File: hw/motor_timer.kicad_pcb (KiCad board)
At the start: 2 copper layers, 15 parts, among them J1 BAT+, J2 BAT-, J3 StartBtn, J4 Motor+, J5 Motor-, Q1 IRF7413, U1 PIC12F1571-I/P

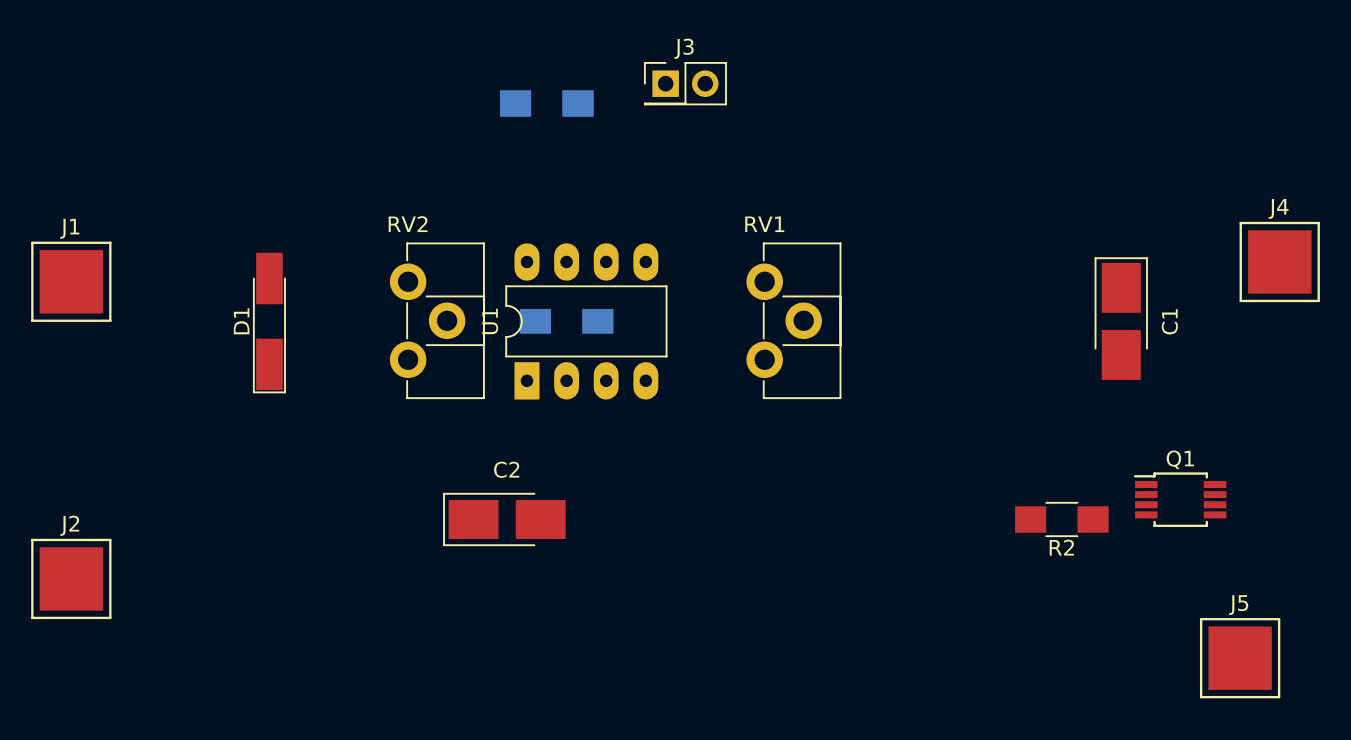
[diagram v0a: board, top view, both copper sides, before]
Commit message: Routed PCB with routes on wrong layers
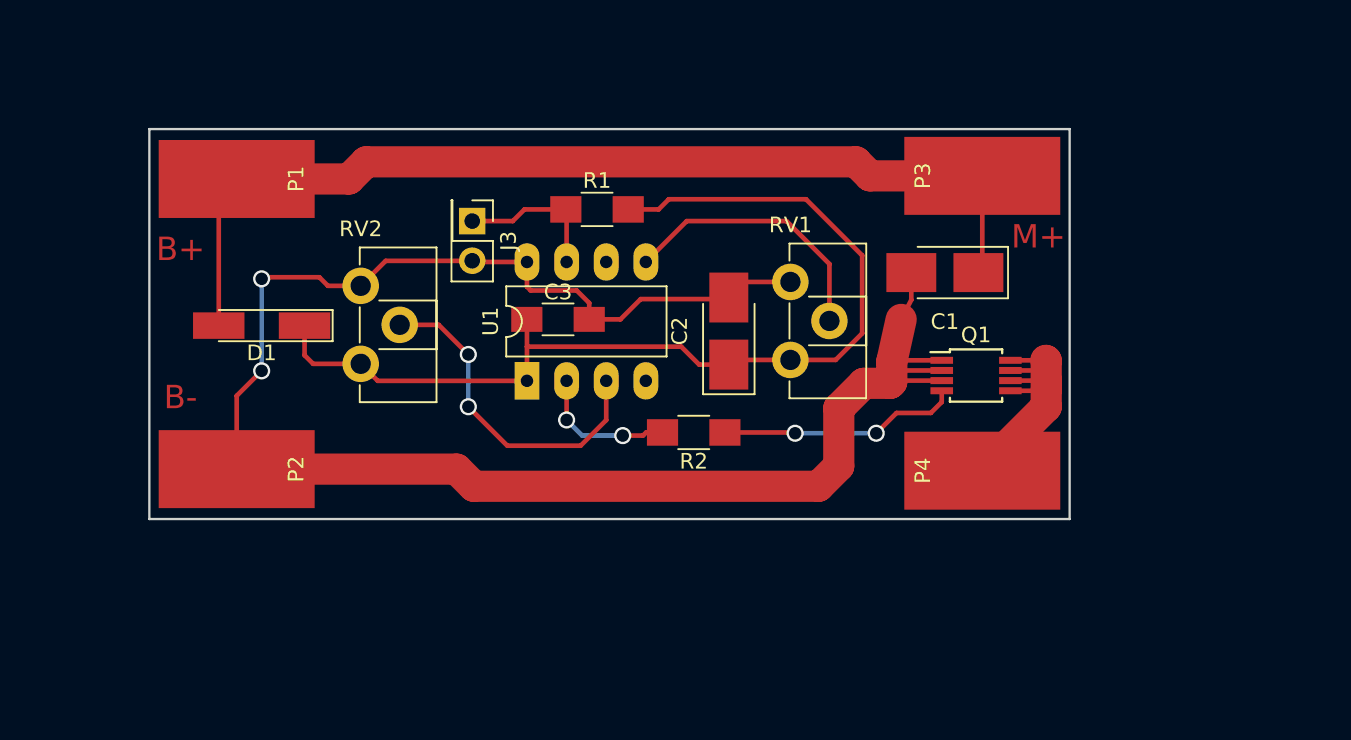
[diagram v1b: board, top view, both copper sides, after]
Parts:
- removed J1: BAT+, SMD_Packages:1Pin
- removed J2: BAT-, SMD_Packages:1Pin
- removed J4: Motor+, SMD_Packages:1Pin
- removed J5: Motor-, SMD_Packages:1Pin
- added P1: BAT+, Wire_Pads:SolderWirePad_single_SMD_5x10mm, F.Cu at (137.6, 91.2)
- added P2: BAT-, Wire_Pads:SolderWirePad_single_SMD_5x10mm, F.Cu at (137.6, 109.8)
- added P3: MOTOR+, Wire_Pads:SolderWirePad_single_SMD_5x10mm, F.Cu at (185.4, 91.0)
- added P4: MOTOR-, Wire_Pads:SolderWirePad_single_SMD_5x10mm, F.Cu at (185.4, 109.9)
- C3, R1: moved to F.Cu
- moved R2 24.3 mm to (166.9, 107.5)
- moved C2 18.7 mm to (169.2, 101.0), turned to 90 degrees
- moved Q1 15.3 mm to (185.0, 103.8)
- moved J3 15.2 mm to (152.7, 93.9), turned to 270 degrees
- moved C1 11.7 mm to (183.0, 97.2), turned to 180 degrees
- moved R1 7.51 mm to (160.7, 93.2), turned to 0 degrees
- moved RV2 3.05 mm to (145.6, 98.0)
- moved RV1 1.65 mm to (173.1, 97.8)
- moved D1 0.57 mm to (139.2, 100.6), turned to 180 degrees
- moved C3 0.57 mm to (158.2, 100.2)
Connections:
- R1 pad 2: Net-(C1-Pad1) -> Net-(C2-Pad1)
- RV1 pad 3: Net-(C1-Pad1) -> Net-(C2-Pad1)
- RV2 pad 3: Net-(C1-Pad1) -> Net-(C2-Pad1)
- U1 pad 4: Net-(U1-Pad4) -> (no net)
- U1 pad 6: Net-(U1-Pad6) -> (no net)
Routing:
- net GND: track 0.00 -> 117.2 mm, vias 0 -> 2
- net Net-(C2-Pad1): track 0.00 -> 65.4 mm
- net Net-(C1-Pad1): track 0.00 -> 64.8 mm
- net Net-(RV2-Pad2): track 0.00 -> 21.6 mm, vias 0 -> 2
- net Net-(P4-Pad1): track 0.00 -> 18.3 mm
- net Net-(RV1-Pad2): track 0.00 -> 17.6 mm
- net Net-(Q1-Pad4): track 0.00 -> 15.5 mm, vias 0 -> 2
- net Net-(J3-Pad1): track 0.00 -> 9.70 mm
- net Net-(R2-Pad2): track 0.00 -> 9.16 mm, vias 0 -> 2
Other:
- board outline added: 59 x 25 mm
- net class Default: clearance 0.2 -> 0; trace_width 0.25 -> 0.3; via_dia 0.6 -> 1.1; via_drill 0.4 -> 0.8
- net class Power added: clearance 0, trace_width 1, via_dia 1.1, via_drill 0.8
- rule trace_clearance: 0.2 -> 0
- board text added: "B+"
- board text added: "B-"
- board text added: "M+"

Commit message: A bit broken small PCB
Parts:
- added J3: StartBtn, Pin_Headers:Pin_Header_Straight_2x01_Pitch2.54mm, F.Cu at (157.3, 120.2)
- added P1: BAT+, Wire_Pads:SolderWirePad_single_SMD_5x10mm, F.Cu at (157.3, 120.2)
- added P2: BAT-, Wire_Pads:SolderWirePad_single_SMD_5x10mm, F.Cu at (157.3, 120.2)
- added P3: MOTOR+, Wire_Pads:SolderWirePad_single_SMD_5x10mm, F.Cu at (157.3, 120.2)
- added P4: MOTOR-, Wire_Pads:SolderWirePad_single_SMD_5x10mm, F.Cu at (157.3, 120.2)
- added P5: Prog, Connectors:GS3, B.Cu at (145.0, 99.4)
- added Throt: Throt, Potentiometers:Potentiometer_Trimmer_Vishay_TS53YJ, F.Cu at (167.1, 99.4)
- added Time: Time, Potentiometers:Potentiometer_Trimmer_Vishay_TS53YJ, F.Cu at (151.0, 99.6)
- C3, D1, Q1, R1, R2: moved to B.Cu
- RV1, RV2: footprint Potentiometers:Potentiometer_Trimmer_ACP_CA9h2.5_Vertical_Px2.5mm_Py5.0mm -> Potentiometers:Potentiometer_Trimmer_Vishay_TS53YJ
- U1: footprint Housings_DIP:DIP-8_W7.62mm_LongPads -> Housings_SOIC:SOIC-8_3.9x4.9mm_Pitch1.27mm; moved to B.Cu
- moved C1 36.8 mm to (146.3, 99.5), turned to 270 degrees
- moved RV1 27.4 mm to (157.3, 120.2)
- moved RV2 25.1 mm to (157.3, 120.2)
- moved D1 22.2 mm to (159.5, 91.5)
- moved Mot- 20.3 mm to (165.3, 107.0)
- moved Mot+ 20.1 mm to (165.3, 92.1)
- moved Q1 19.7 mm to (165.3, 105.0)
- moved Bat- 12.0 mm to (149.3, 107.0)
- moved Bat+ 11.7 mm to (149.3, 92.1)
- moved Start 11.3 mm to (156.9, 104.4)
- moved C2 10.1 mm to (159.2, 98.9), turned to 180 degrees
- moved R1 9.00 mm to (152.1, 95.8), turned to 180 degrees
- moved R2 8.06 mm to (167.2, 99.4), turned to 90 degrees
- moved C3 5.63 mm to (159.4, 94.7), turned to 180 degrees
- moved U1 5.49 mm to (159.3, 99.6), turned to 180 degrees
- renumbered P1 to Bat+, P2 to Bat-, P3 to Mot+, P4 to Mot-, J3 to Start
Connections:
- net Net-(C1-Pad1) renamed +BATT
- net Net-(C2-Pad1) renamed +3V3
- U1 pad 4: (no net) -> Net-(P5-Pad1)
- U1 pad 6: (no net) -> Net-(P5-Pad2)
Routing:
- net GND: track 117.2 -> 60.2 mm, vias 2 -> 1
- net +BATT: track 64.8 -> 26.5 mm, vias 0 -> 1
- net +3V3: track 65.4 -> 41.8 mm, vias 0 -> 1
- net Net-(P5-Pad1): track 0.00 -> 18.7 mm, vias 0 -> 2
- net Net-(RV2-Pad2): track 21.6 -> 5.58 mm, vias 2 -> 1
- net Net-(J3-Pad1): track 9.70 -> 22.2 mm
- net Net-(RV1-Pad2): track 17.6 -> 5.65 mm, vias 0 -> 1
- net Net-(P5-Pad2): track 0.00 -> 11.9 mm
- net Net-(Q1-Pad4): track 15.5 -> 5.52 mm, vias 2 -> 0
- net Net-(R2-Pad2): track 9.16 -> 5.85 mm, vias 2 -> 0
- net Net-(P4-Pad1): track 18.3 -> 15.9 mm, vias 0 -> 1
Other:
- board size 59 x 25 mm -> 27 x 21 mm
- net class Default: clearance 0 -> 0.1778; trace_width 0.3 -> 0.25; via_dia 1.1 -> 0.7; via_drill 0.8 -> 0.4
- net class Power: clearance 0 -> 0.2
- rule trace_clearance: 0 -> 0.1778
- rule trace_min: 0.2 -> 0.1524
- rule via_min_drill: 0.3 -> 0.254
- rule via_min_size: 0.4 -> 0.508
- board text added: "Dat Clk Rst"
- board text added: "Mot tmr v1.0"
- board text added: "v1.0"
- board text removed: "B+"
- board text removed: "B-"
- board text removed: "M+"

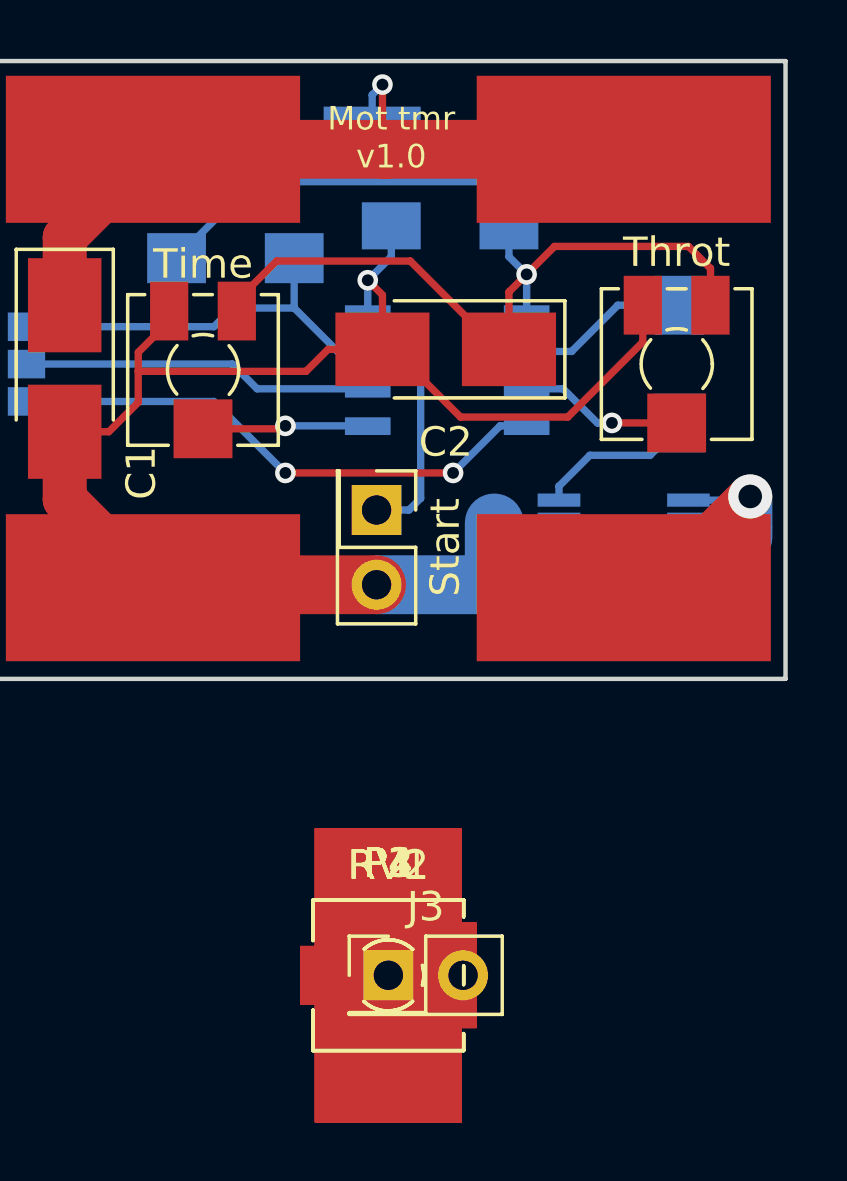
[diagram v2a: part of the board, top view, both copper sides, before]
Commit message: Final version of small PCB. But there are broken referneces betveen schamatic and board.
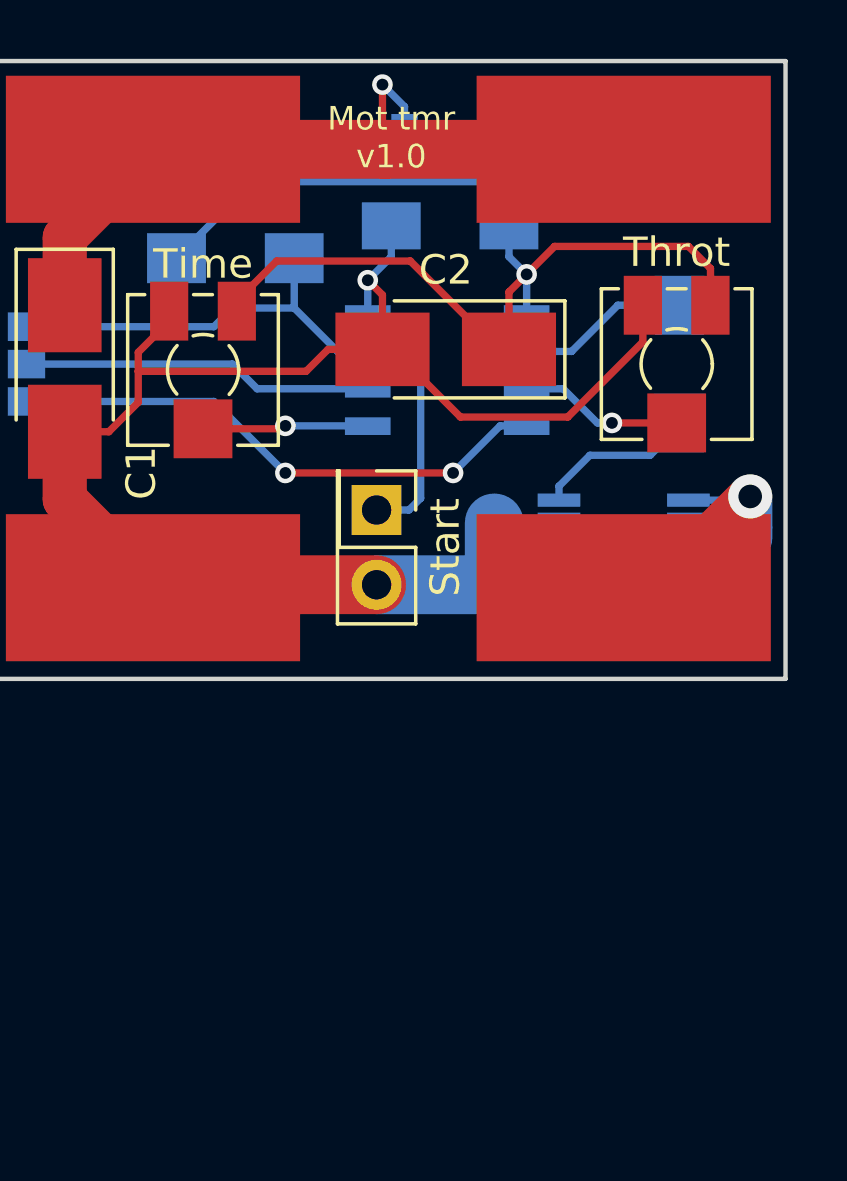
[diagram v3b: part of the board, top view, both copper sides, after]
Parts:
- removed J3: StartBtn, Pin_Headers:Pin_Header_Straight_2x01_Pitch2.54mm
- removed P1: BAT+, Wire_Pads:SolderWirePad_single_SMD_5x10mm
- removed P2: BAT-, Wire_Pads:SolderWirePad_single_SMD_5x10mm
- removed P3: MOTOR+, Wire_Pads:SolderWirePad_single_SMD_5x10mm
- removed P4: MOTOR-, Wire_Pads:SolderWirePad_single_SMD_5x10mm
- removed RV1: Time, Potentiometers:Potentiometer_Trimmer_Vishay_TS53YJ
- removed RV2: Throt, Potentiometers:Potentiometer_Trimmer_Vishay_TS53YJ
- D1: footprint Diodes_SMD:D_MiniMELF_Handsoldering -> Diodes_SMD:D_SOD-123
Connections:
- Throt pad 2: Net-(RV2-Pad2) -> (no net)
- Time pad 2: Net-(RV1-Pad2) -> (no net)
- U1 pad 3: Net-(RV2-Pad2) -> Net-(Throt1-Pad2)
- U1 pad 5: Net-(RV1-Pad2) -> Net-(Time1-Pad2)
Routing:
- net Net-(Time1-Pad2): track 0.00 -> 5.65 mm, vias 0 -> 1
- net Net-(RV1-Pad2): track 5.65 -> 0.00 mm, vias 1 -> 0
- net Net-(Throt1-Pad2): track 0.00 -> 5.58 mm, vias 0 -> 1
- net Net-(RV2-Pad2): track 5.58 -> 0.00 mm, vias 1 -> 0
- net +3V3: track 41.8 -> 41.1 mm

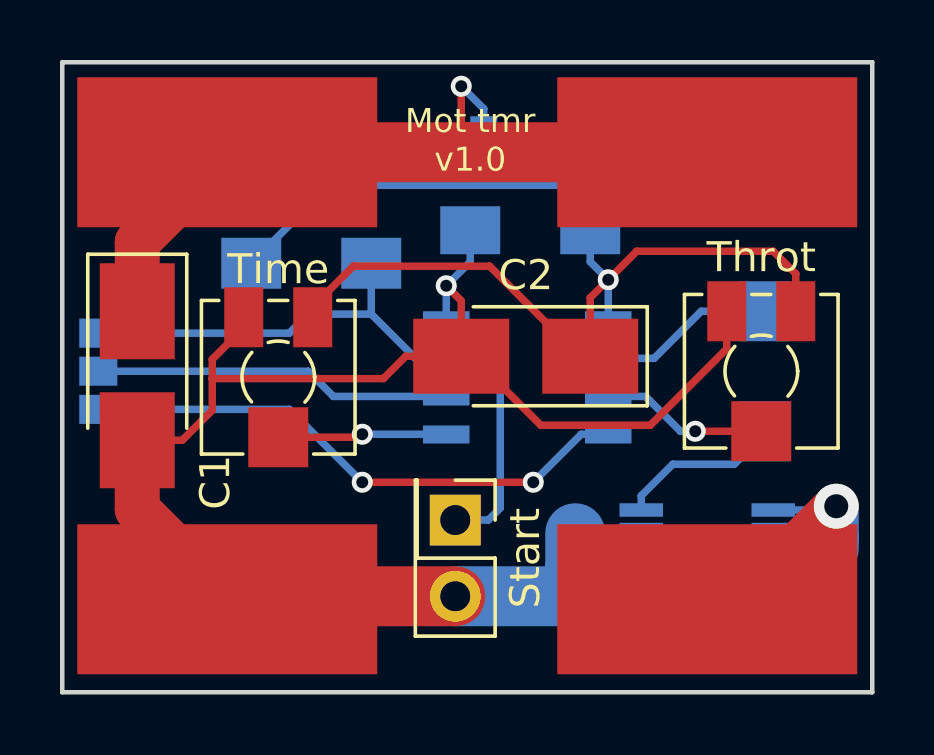
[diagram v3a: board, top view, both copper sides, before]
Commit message: XS PCB
Fixed references between schm and pcb
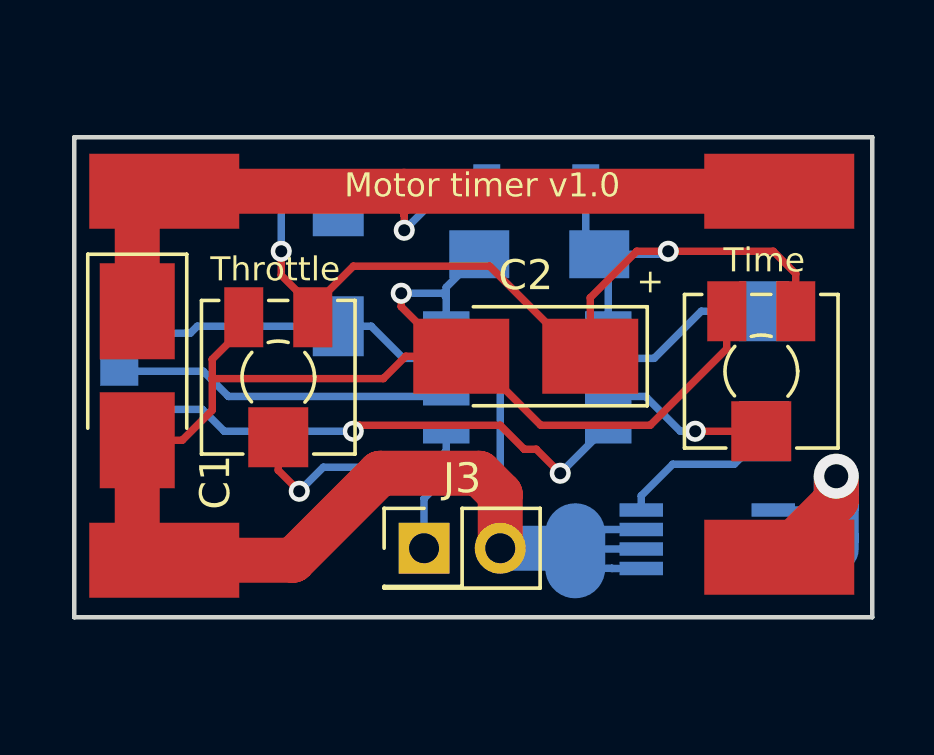
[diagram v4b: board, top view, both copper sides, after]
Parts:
- removed Bat+: BAT+, Wire_Pads:SolderWirePad_single_SMD_5x10mm
- removed Bat-: BAT-, Wire_Pads:SolderWirePad_single_SMD_5x10mm
- removed Mot+: MOTOR+, Wire_Pads:SolderWirePad_single_SMD_5x10mm
- removed Mot-: MOTOR-, Wire_Pads:SolderWirePad_single_SMD_5x10mm
- removed Start: StartBtn, Pin_Headers:Pin_Header_Straight_2x01_Pitch2.54mm
- added J3: StartBtn, Pin_Headers:Pin_Header_Straight_2x01_Pitch2.54mm, F.Cu at (155.9, 105.3)
- added P1: BAT+, motor_timer:SMT Solder PAD 2.5x5mm, F.Cu at (147.2, 93.4)
- added P2: BAT-, motor_timer:SMT Solder PAD 2.5x5mm, F.Cu at (147.2, 105.7)
- added P3: MOTOR+, motor_timer:SMT Solder PAD 2.5x5mm, F.Cu at (167.7, 93.4)
- added eP4: MOTOR-, motor_timer:SMT Solder PAD 2.5x5mm, F.Cu at (167.7, 105.6)
- T1: renamed from Time; value Time -> Throt
- T2: renamed from Throt; value Throt -> Time
- moved D1 1.60 mm to (159.6, 93.1)
- moved R1 0.91 mm to (153.0, 95.9), turned to 90 degrees
- moved C3 0.85 mm to (159.7, 95.5)
- moved P5 0.70 mm to (145.7, 99.4)
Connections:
- net Net-(P4-Pad1) renamed /M-
- net Net-(R2-Pad2) renamed /TGate
- T1 pad 2: (no net) -> /Throt
- T2 pad 2: (no net) -> /Time
- U1 pad 3: Net-(Throt1-Pad2) -> /Time
- U1 pad 5: Net-(Time1-Pad2) -> /Throt
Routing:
- net /Throt: track 0.00 -> 8.11 mm, vias 0 -> 1
- net +3V3: track 41.1 -> 35.3 mm, vias 1 -> 2
- net Net-(Time1-Pad2): track 5.65 -> 0.00 mm, vias 1 -> 0
- net Net-(Throt1-Pad2): track 5.58 -> 0.00 mm, vias 1 -> 0
- net /Time: track 0.00 -> 5.58 mm, vias 0 -> 1
- net GND: track 60.2 -> 64.2 mm
- net +BATT: track 26.7 -> 29.1 mm
- net Net-(J3-Pad1): track 22.2 -> 21.0 mm
- net /M-: track 15.9 -> 14.8 mm
- net Net-(P5-Pad2): track 11.9 -> 11.2 mm
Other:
- board size 27 x 21 mm -> 26.6 x 16 mm
- board text added: "+"
- board text added: "3,0-5,0V Max 3A"
- board text added: "Bat+"
- board text added: "Bat-"
- board text added: "M-"
- board text added: "Mot+"
- board text added: "Motor timer v1.0"
- board text added: "Throttle"
- board text added: "Time"
- board text removed: "Mot tmr v1.0"
